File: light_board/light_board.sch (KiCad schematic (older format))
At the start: 14 parts, among them J1 CONN_01X02, J2 Led_Connector, J3 Power_Connector, Q1 FDC658AP, U1 LM3409MY

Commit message: finished wiring pcb
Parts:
- added D2: LED, LEDs:LED_0603, symbol LED
- added Rled1: 1kR, Resistors_SMD:R_0603, symbol R
- Cin1: renamed from Cin; footprint Capacitors_THT:CP_Radial_Tantal_D5.0mm_P2.50mm -> Capacitors_SMD:C_0603
- D1: footprint Diodes_THT:D_5KPW_P7.62mm_Vertical_AnodeUp -> Diodes_SMD:D_0603
- J1: footprint Pin_Headers:Pin_Header_Straight_1x02_Pitch2.54mm -> Connectors_Terminal_Blocks:TerminalBlock_Pheonix_MPT-2.54mm_2pol
- J2: footprint Connectors_Terminal_Blocks:TerminalBlock_Philmore_TB132_02x5mm_Straight -> Connectors_Terminal_Blocks:TerminalBlock_Pheonix_PT-3.5mm_2pol
- J3: footprint Connectors_Terminal_Blocks:TerminalBlock_Pheonix_MPT-2.54mm_2pol -> Connectors_Terminal_Blocks:TerminalBlock_Pheonix_PT-3.5mm_2pol
- Q1: footprint footprints:FDC658AP FDC658AP -> footprints:FDC658AP_FDC658AP
- Rsns1: renamed from Rsns; footprint Resistors_THT:R_Axial_DIN0614_L14.3mm_D5.7mm_P15.24mm_Horizontal -> Resistors_SMD:R_0603
- renumbered Cf to Cf1, Coff to Coff1, Roff to Roff1
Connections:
- net GND: now also D2.1 (K)
- net PGATE: now also Rled1.1
- net notUsed: now reaches J1.1 (P1), U1.2 (IADJ)
- net inputSignal: now reaches J1.2 (P2), U1.3 (EN)
- net LEDVcc: now reaches J2.1, L1.2, Roff1.1
- net diodeToLToPMOS: now reaches D1.1, L1.1, Q1.1 (D), Q1.2 (D), Q1.5 (D), Q1.6 (D)
- new net: D2.2 (A), Rled1.2
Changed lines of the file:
@@
 LIBS:contrib
 LIBS:valves
-LIBS:agg-kicad
 LIBS:cauv_lib
 LIBS:light_board-cache
@@
 F 0 "J1" H 3650 3600 50  0000 C CNN
 F 1 "CONN_01X02" V 3750 3450 50  0000 C CNN
-F 2 "Pin_Headers:Pin_Header_Straight_1x02_Pitch2.54mm" H 3650 3450 50  0001 C CNN
+F 2 "Connectors_Terminal_Blocks:TerminalBlock_Pheonix_MPT-2.54mm_2pol" H 3650 3450 50  0001 C CNN
 F 3 "" H 3650 3450 50  0001 C CNN
 	1    3650 3450
@@
 $EndComp
 $Comp
-L C Cf
+L C Cf1
 U 1 1 58D54246
 P 4950 2800
-F 0 "Cf" H 4975 2900 50  0000 L CNN
+F 0 "Cf1" H 4975 2900 50  0000 L CNN
 F 1 "1uF" H 4975 2700 50  0000 L CNN
 F 2 "Capacitors_SMD:C_0603" H 4988 2650 50  0001 C CNN
@@
 $EndComp
 $Comp
-L GND #PWR04
+L GND #PWR02
 U 1 1 58D54D16
 P 7700 2500
-F 0 "#PWR04" H 7700 2250 50  0001 C CNN
+F 0 "#PWR02" H 7700 2250 50  0001 C CNN
 F 1 "GND" H 7700 2350 50  0000 C CNN
 F 2 "" H 7700 2500 50  0001 C CNN
@@
 CSP
 $Comp
-L C Coff
+L C Coff1
 U 1 1 58D550FA
 P 7550 4700
-F 0 "Coff" H 7575 4800 50  0000 L CNN
+F 0 "Coff1" H 7575 4800 50  0000 L CNN
 F 1 "470pF" H 7575 4600 50  0000 L CNN
 F 2 "Capacitors_SMD:C_0603" H 7588 4550 50  0001 C CNN
@@
 $EndComp
 $Comp
-L R Roff
+L R Roff1
 U 1 1 58D55135
 P 7900 4450
-F 0 "Roff" V 7980 4450 50  0000 C CNN
+F 0 "Roff1" V 7980 4450 50  0000 C CNN
 F 1 "13k" V 7900 4450 50  0000 C CNN
 F 2 "Resistors_SMD:R_0603" V 7830 4450 50  0001 C CNN
@@
 F 0 "D1" V 8700 4670 50  0000 C CNN
 F 1 "SCHOTTKY" H 8700 4530 50  0000 C CNN
-F 2 "Diodes_THT:D_5KPW_P7.62mm_Vertical_AnodeUp" H 8600 4570 50  0001 C CNN
+F 2 "Diodes_SMD:D_0603" H 8600 4570 50  0001 C CNN
 F 3 "" H 8700 4670 50  0001 C CNN
 	1    8650 4600
@@
 $EndComp
 $Comp
-L GND #PWR05
+L GND #PWR03
 U 1 1 58D55462
 P 8650 4850
-F 0 "#PWR05" H 8650 4600 50  0001 C CNN
+F 0 "#PWR03" H 8650 4600 50  0001 C CNN
 F 1 "GND" H 8650 4700 50  0000 C CNN
 F 2 "" H 8650 4850 50  0001 C CNN
@@
 $EndComp
 $Comp
-L GND #PWR06
+L GND #PWR04
 U 1 1 58D55663
 P 7550 4950
-F 0 "#PWR06" H 7550 4700 50  0001 C CNN
+F 0 "#PWR04" H 7550 4700 50  0001 C CNN
 F 1 "GND" H 7550 4800 50  0000 C CNN
 F 2 "" H 7550 4950 50  0001 C CNN
@@
 $EndComp
 $Comp
-L R Rsns
+L R Rsns1
 U 1 1 58D55809
 P 8250 3300
-F 0 "Rsns" V 8330 3300 50  0000 C CNN
+F 0 "Rsns1" V 8330 3300 50  0000 C CNN
 F 1 "0.15R" V 8250 3300 50  0000 C CNN
-F 2 "Resistors_THT:R_Axial_DIN0614_L14.3mm_D5.7mm_P15.24mm_Horizontal" V 8180 3300 50  0001 C CNN
+F 2 "Resistors_SMD:R_0603" V 8180 3300 50  0001 C CNN
 F 3 "" H 8250 3300 50  0001 C CNN
 	1    8250 3300
@@
 $EndComp
 $Comp
-L CP Cin
+L CP Cin1
 U 1 1 58D559B3
 P 8750 3250
-F 0 "Cin" H 8775 3350 50  0000 L CNN
+F 0 "Cin1" H 8775 3350 50  0000 L CNN
 F 1 "5uF" H 8775 3150 50  0000 L CNN
-F 2 "Capacitors_THT:CP_Radial_Tantal_D5.0mm_P2.50mm" H 8788 3100 50  0001 C CNN
+F 2 "Capacitors_SMD:C_0603" H 8788 3100 50  0001 C CNN
 F 3 "" H 8750 3250 50  0001 C CNN
 	1    8750 3250
@@
 $EndComp
 $Comp
-L GND #PWR07
+L GND #PWR05
 U 1 1 58D55A22
 P 8750 3500
-F 0 "#PWR07" H 8750 3250 50  0001 C CNN
+F 0 "#PWR05" H 8750 3250 50  0001 C CNN
 F 1 "GND" H 8750 3350 50  0000 C CNN
 F 2 "" H 8750 3500 50  0001 C CNN
@@
 F 0 "J2" H 7700 5750 50  0000 C TNN
 F 1 "Led_Connector" V 7550 5500 50  0000 C TNN
-F 2 "Connectors_Terminal_Blocks:TerminalBlock_Philmore_TB132_02x5mm_Straight" H 7700 5275 50  0001 C CNN
+F 2 "Connectors_Terminal_Blocks:TerminalBlock_Pheonix_PT-3.5mm_2pol" H 7700 5275 50  0001 C CNN
 F 3 "" H 7675 5500 50  0001 C CNN
 	1    7700 5500
@@
 $EndComp
 $Comp
-L GND #PWR08
+L GND #PWR06
 U 1 1 58D57599
 P 8150 5600
-F 0 "#PWR08" H 8150 5350 50  0001 C CNN
+F 0 "#PWR06" H 8150 5350 50  0001 C CNN
 F 1 "GND" H 8150 5450 50  0000 C CNN
 F 2 "" H 8150 5600 50  0001 C CNN
@@
 F 0 "Q1" H 8400 3950 50  0000 L CNN
 F 1 "FDC658AP" H 8400 3850 50  0000 L CNN
-F 2 "footprints:FDC658APFDC658AP" H 8150 3950 50  0001 L CNN
+F 2 "footprints:FDC658AP_FDC658AP" H 8150 3950 50  0001 L CNN
 F 3 "0.21 USD" H 8150 3950 50  0001 L CNN
 F 4 "Fairchild Semiconductor" H 8150 3950 50  0001 L CNN "MF"
@@
 F 0 "J3" H 9300 3400 50  0000 C TNN
 F 1 "Power_Connector" V 9150 3150 50  0000 C TNN
-F 2 "Connectors_Terminal_Blocks:TerminalBlock_Pheonix_MPT-2.54mm_2pol" H 9300 2925 50  0001 C CNN
+F 2 "Connectors_Terminal_Blocks:TerminalBlock_Pheonix_PT-3.5mm_2pol" H 9300 2925 50  0001 C CNN
 F 3 "" H 9275 3150 50  0001 C CNN
 	1    9300 3150
@@
 Text Notes 9250 4100 0    60   ~ 0
 pmos has been flipped so that the source is connected to the higher voltage
+$Comp
+L VCC #PWR07
+U 1 1 59CB85B1
+P 9000 3050
+F 0 "#PWR07" H 9000 2900 50  0001 C CNN
+F 1 "VCC" H 9000 3200 50  0000 C CNN
+F 2 "" H 9000 3050 50  0001 C CNN
+F 3 "" H 9000 3050 50  0001 C CNN
+	1    9000 3050
+	1    0    0    -1
+$EndComp
+Text Label 4050 3400 0    60   ~ 0
+inputSignal
+Text Label 4100 3500 0    60   ~ 0
+notUsed
+Text Label 8100 5400 0    60   ~ 0
+LEDVcc
+Text Label 8000 5600 0    60   ~ 0
+LEDgnd
+Text Label 8450 4450 0    60   ~ 0
+diodeToLToPMOS
+$Comp
+L PWR_FLAG #FLG08
+U 1 1 59CB9953
+P 3700 1850
+F 0 "#FLG08" H 3700 1925 50  0001 C CNN
+F 1 "PWR_FLAG" H 3700 2000 50  0000 C CNN
+F 2 "" H 3700 1850 50  0001 C CNN
+F 3 "" H 3700 1850 50  0001 C CNN
+	1    3700 1850
+	1    0    0    -1
+$EndComp
+$Comp
+L PWR_FLAG #FLG09
+U 1 1 59CB99FF
+P 4200 1850
+F 0 "#FLG09" H 4200 1925 50  0001 C CNN
+F 1 "PWR_FLAG" H 4200 2000 50  0000 C CNN
+F 2 "" H 4200 1850 50  0001 C CNN
+F 3 "" H 4200 1850 50  0001 C CNN
+	1    4200 1850
+	1    0    0    -1
+$EndComp
+$Comp
+L VCC #PWR010
+U 1 1 59CB9A28
+P 3700 2150
+F 0 "#PWR010" H 3700 2000 50  0001 C CNN
+F 1 "VCC" H 3700 2300 50  0000 C CNN
+F 2 "" H 3700 2150 50  0001 C CNN
+F 3 "" H 3700 2150 50  0001 C CNN
+	1    3700 2150
+	1    0    0    1
+$EndComp
+$Comp
+L GND #PWR011
+U 1 1 59CB9A58
+P 4200 2150
+F 0 "#PWR011" H 4200 1900 50  0001 C CNN
+F 1 "GND" H 4200 2000 50  0000 C CNN
+F 2 "" H 4200 2150 50  0001 C CNN
+F 3 "" H 4200 2150 50  0001 C CNN
+	1    4200 2150
+	1    0    0    -1
+$EndComp
+Wire Wire Line
+	4200 1850 4200 2150
+Wire Wire Line
+	3700 2150 3700 1850
+$Comp
+L GND #PWR012
+U 1 1 59CC10D5
+P 6750 3500
+F 0 "#PWR012" H 6750 3250 50  0001 C CNN
+F 1 "GND" H 6750 3350 50  0000 C CNN
+F 2 "" H 6750 3500 50  0001 C CNN
+F 3 "" H 6750 3500 50  0001 C CNN
+	1    6750 3500
+	1    0    0    -1
+$EndComp
+$Comp
+L LED D2
+U 1 1 59CC1105
+P 6750 3350
+F 0 "D2" H 6750 3450 50  0000 C CNN
+F 1 "LED" H 6750 3250 50  0000 C CNN
+F 2 "LEDs:LED_0603" H 6750 3350 50  0001 C CNN
+F 3 "" H 6750 3350 50  0001 C CNN
+	1    6750 3350
+	0    -1   -1   0
+$EndComp
+$Comp
+L R Rled1
+U 1 1 59CC23F4
+P 6750 3050
+F 0 "Rled1" V 6830 3050 50  0000 C CNN
+F 1 "1kR" V 6750 3050 50  0000 C CNN
+F 2 "Resistors_SMD:R_0603" V 6680 3050 50  0001 C CNN
+F 3 "" H 6750 3050 50  0001 C CNN
+	1    6750 3050
+	1    0    0    -1
+$EndComp
+Text Label 6750 2900 0    60   ~ 0
+PGATE
 $EndSCHEMATC

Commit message: light_board finished
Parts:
- D1: footprint Diodes_SMD:D_0603 -> Diodes_THT:D_T-1_P5.08mm_Horizontal
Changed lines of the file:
@@
 F 0 "D1" V 8700 4670 50  0000 C CNN
 F 1 "SCHOTTKY" H 8700 4530 50  0000 C CNN
-F 2 "Diodes_SMD:D_0603" H 8600 4570 50  0001 C CNN
+F 2 "Diodes_THT:D_T-1_P5.08mm_Horizontal" H 8600 4570 50  0001 C CNN
 F 3 "" H 8700 4670 50  0001 C CNN
 	1    8650 4600

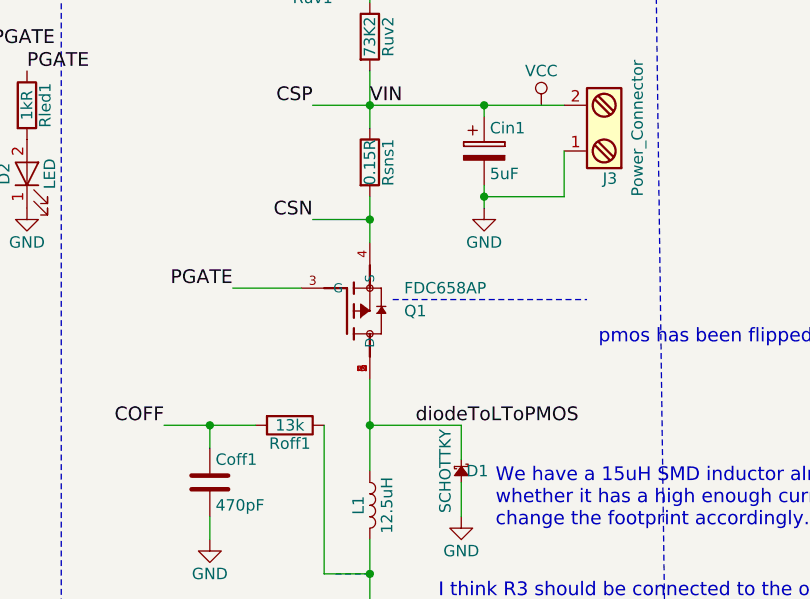
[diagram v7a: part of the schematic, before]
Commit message: changed footprints of resistor and diode
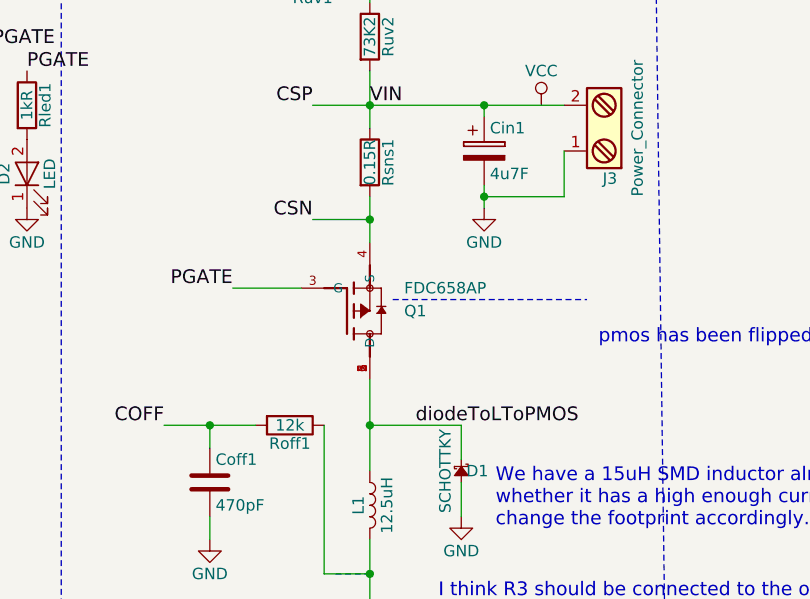
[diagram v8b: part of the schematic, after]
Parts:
- Cin1: value 5uF -> 4u7F
- L1: footprint Inductors_THT:L_Axial_L16.0mm_D6.3mm_P25.40mm_Horizontal_Fastron_VHBCC -> Inductors_SMD:L_Wuerth_WE-PD2-Typ-XL
- Roff1: value 13k -> 12k
- Rsns1: footprint Resistors_SMD:R_0603 -> Resistors_SMD:R_0805
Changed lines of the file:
@@
 P 7900 4450
 F 0 "Roff1" V 7980 4450 50  0000 C CNN
-F 1 "13k" V 7900 4450 50  0000 C CNN
+F 1 "12k" V 7900 4450 50  0000 C CNN
 F 2 "Resistors_SMD:R_0603" V 7830 4450 50  0001 C CNN
 F 3 "" H 7900 4450 50  0001 C CNN
@@
 F 0 "L1" V 8200 4800 50  0000 C CNN
 F 1 "12.5uH" V 8325 4800 50  0000 C CNN
-F 2 "Inductors_THT:L_Axial_L16.0mm_D6.3mm_P25.40mm_Horizontal_Fastron_VHBCC" H 8250 4800 50  0001 C CNN
+F 2 "Inductors_SMD:L_Wuerth_WE-PD2-Typ-XL" H 8250 4800 50  0001 C CNN
 F 3 "" H 8250 4800 50  0001 C CNN
 	1    8250 4800
@@
 F 0 "Rsns1" V 8330 3300 50  0000 C CNN
 F 1 "0.15R" V 8250 3300 50  0000 C CNN
-F 2 "Resistors_SMD:R_0603" V 8180 3300 50  0001 C CNN
+F 2 "Resistors_SMD:R_0805" V 8180 3300 50  0001 C CNN
 F 3 "" H 8250 3300 50  0001 C CNN
 	1    8250 3300
@@
 P 8750 3250
 F 0 "Cin1" H 8775 3350 50  0000 L CNN
-F 1 "5uF" H 8775 3150 50  0000 L CNN
+F 1 "4u7F" H 8775 3150 50  0000 L CNN
 F 2 "Capacitors_SMD:C_0603" H 8788 3100 50  0001 C CNN
 F 3 "" H 8750 3250 50  0001 C CNN
